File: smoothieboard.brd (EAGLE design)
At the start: 105.1 x 105.1 mm, 236 parts, among them IC1 LPC1769, IC10 LM1117-3.3V, IC11 78L12F, IC2 A4982, IC3 A4982, IC4 MCP44X1, IC5 A4982, IC6 A4982, J10 POWER_JACKSMD, J5 POWER_JACKSMD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

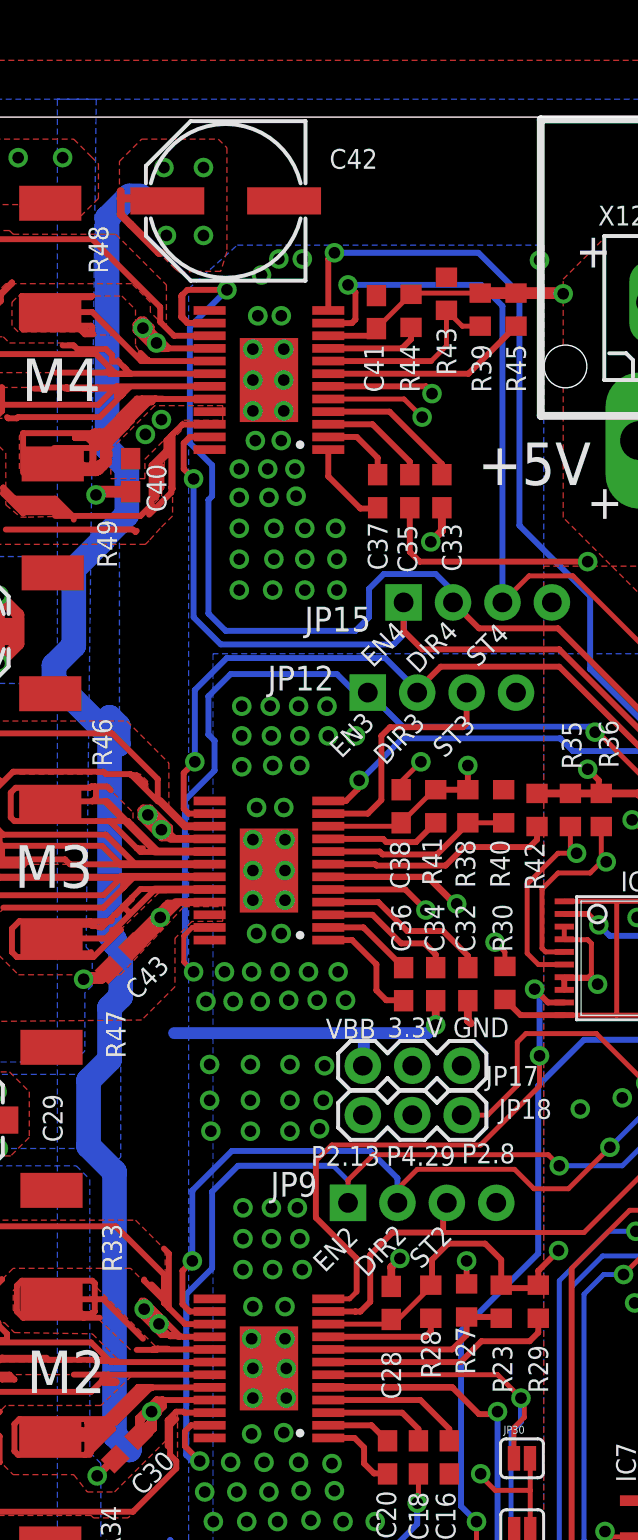
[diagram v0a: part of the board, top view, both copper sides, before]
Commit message: Moved C34 to allow heatsink to reach all four drivers from side
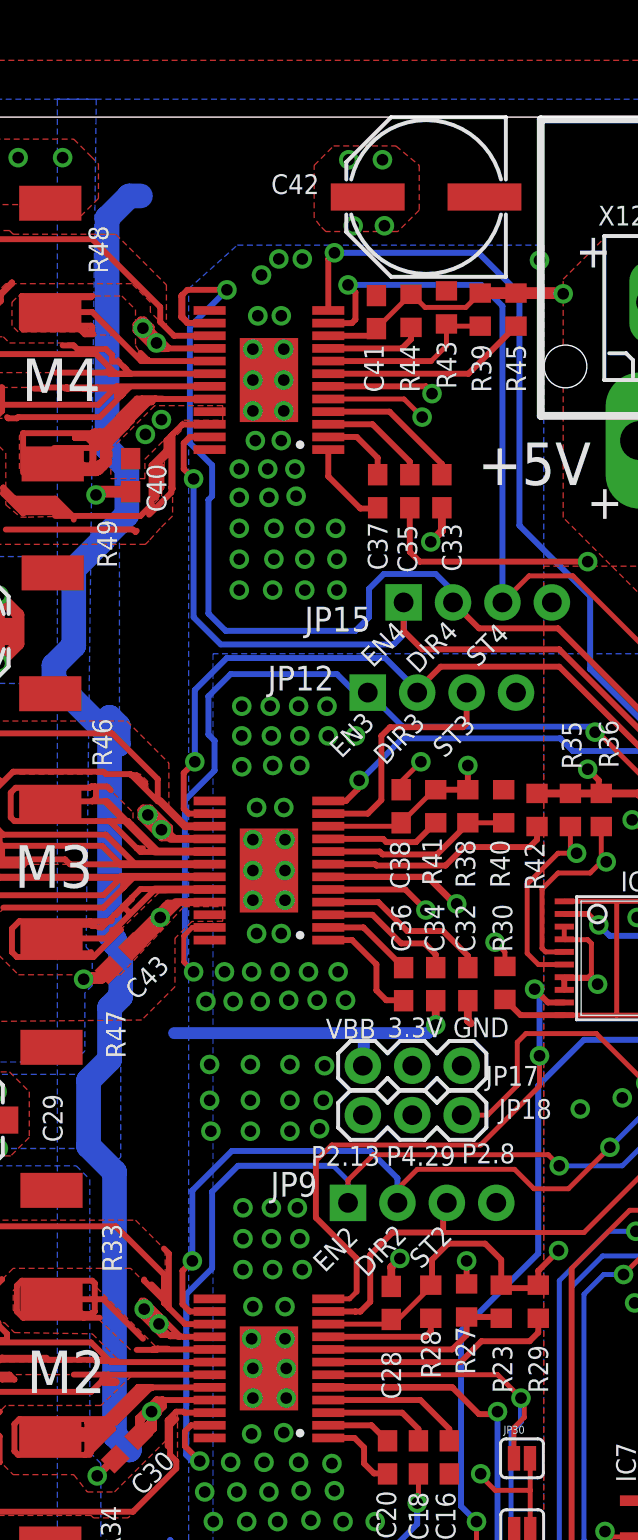
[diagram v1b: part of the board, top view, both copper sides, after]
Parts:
- moved C42 10.3 mm to (32.0, 101.0)
- moved R43 0.70 mm to (33.0, 95.3)
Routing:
- net VBB: track 332.1 -> 326.9 mm
- net N$53: track 10.3 -> 9.30 mm
- net 3.3V: track 249.6 -> 250.2 mm
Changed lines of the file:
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@@
 <setting verticaltext="up"/>
 </settings>
-<grid distance="0.25" unitdist="mm" unit="mm" style="dots" multiple="4" display="no" altdistance="0.0635" altunitdist="mm" altunit="mm"/>
+<grid distance="0.1" unitdist="mm" unit="mm" style="dots" multiple="4" display="no" altdistance="0.0635" altunitdist="mm" altunit="mm"/>
 <layers>
 <layer number="1" name="Top" color="4" fill="1" visible="yes" active="yes"/>
-<layer number="2" name="Route2" color="2" fill="1" visible="yes" active="yes"/>
+<layer number="2" name="Route2" color="2" fill="1" visible="no" active="yes"/>
 <layer number="3" name="Route3" color="4" fill="3" visible="no" active="no"/>
 <layer number="4" name="Route4" color="1" fill="4" visible="no" active="no"/>
@@
 <layer number="13" name="Route13" color="4" fill="5" visible="no" active="no"/>
 <layer number="14" name="Route14" color="1" fill="6" visible="no" active="no"/>
-<layer number="15" name="Route15" color="5" fill="1" visible="yes" active="yes"/>
+<layer number="15" name="Route15" color="5" fill="1" visible="no" active="yes"/>
 <layer number="16" name="Bottom" color="1" fill="1" visible="yes" active="yes"/>
 <layer number="17" name="Pads" color="2" fill="1" visible="yes" active="yes"/>
@@
 <attribute name="VALUE" x="29.9085" y="96.5835" size="1.27" layer="27" rot="R90"/>
 </element>
-<element name="R43" library="resistor" package="R0603" value="10K" x="33" y="96" smashed="yes" rot="R90">
-<attribute name="NAME" x="33.508" y="91.809" size="1.016" layer="25" rot="R90"/>
-<attribute name="VALUE" x="33.254" y="97.778" size="1.27" layer="27" rot="R90"/>
+<element name="R43" library="resistor" package="R0603" value="10K" x="33" y="95.3" smashed="yes" rot="R90">
+<attribute name="NAME" x="33.508" y="91.109" size="1.016" layer="25" rot="R90"/>
+<attribute name="VALUE" x="33.254" y="97.078" size="1.27" layer="27" rot="R90"/>
 </element>
 <element name="C33" library="rcl" package="C0603" value=".22uF" x="32.766" y="85.852" smashed="yes" rot="R90">
@@
 <attribute name="VALUE" x="5.126" y="76.101" size="0.4064" layer="27"/>
 </element>
-<element name="C42" library="SparkFun" package="PANASONIC_E" value="100uF" x="21.6535" y="100.7745" smashed="yes" rot="R180">
-<attribute name="NAME" x="26.9875" y="102.4255" size="1.016" layer="25"/>
-<attribute name="VALUE" x="22.9235" y="103.3145" size="0.4064" layer="27" rot="R180"/>
+<element name="C42" library="SparkFun" package="PANASONIC_E" value="100uF" x="31.9535" y="100.9745" smashed="yes" rot="R180">
+<attribute name="NAME" x="23.9875" y="101.1255" size="1.016" layer="25"/>
+<attribute name="VALUE" x="33.2235" y="103.5145" size="0.4064" layer="27" rot="R180"/>
 </element>
 <element name="U1" library="SparkFun" package="MICRO-SD-SOCKET-PP" value="USD-SOCKETNEW" x="42.037" y="16.002" rot="R180"/>
@@
 <wire x1="31.1785" y1="95.973" x2="31.164" y2="95.973" width="0.254" layer="1"/>
 <wire x1="31.164" y1="95.973" x2="29.4005" y2="94.2095" width="0.254" layer="1"/>
-<wire x1="31.242" y1="96.0365" x2="34.7345" y2="96.0365" width="0.254" layer="1"/>
 <wire x1="71.15" y1="43" x2="70.94" y2="43" width="0.254" layer="1"/>
 <wire x1="70.94" y1="43" x2="69.7865" y2="41.8465" width="0.254" layer="1"/>
@@
 <wire x1="96.25" y1="14.611" x2="94.551" y2="14.611" width="0.6096" layer="1"/>
 <wire x1="94.551" y1="14.611" x2="94.2865" y2="14.3465" width="0.6096" layer="1"/>
+<wire x1="31.242" y1="96.0365" x2="31.242" y2="95.958" width="0.254" layer="1"/>
+<wire x1="31.242" y1="95.958" x2="31.9" y2="95.3" width="0.254" layer="1"/>
+<wire x1="31.9" y1="95.3" x2="33.998" y2="95.3" width="0.254" layer="1"/>
+<wire x1="33.998" y1="95.3" x2="34.7345" y2="96.0365" width="0.254" layer="1"/>
 </signal>
 <signal name="AVCC">
@@
 <vertex x="93" y="57.5"/>
 </polygon>
-<via x="20.5105" y="102.489" extent="1-16" drill="0.6"/>
-<via x="18.4785" y="102.489" extent="1-16" drill="0.6"/>
-<via x="20.5105" y="98.9965" extent="1-16" drill="0.6"/>
-<via x="18.6055" y="98.9965" extent="1-16" drill="0.6"/>
-<polygon width="0.3048" layer="1">
-<vertex x="20.066" y="97.155"/>
-<vertex x="19.304" y="97.0915"/>
-<vertex x="19.05" y="97.282"/>
-<vertex x="16.1925" y="100.1395"/>
-<vertex x="16.1925" y="102.8065"/>
-<vertex x="17.3355" y="103.9495"/>
-<vertex x="21.2725" y="103.9495"/>
-<vertex x="21.717" y="103.505"/>
-<vertex x="21.717" y="98.171"/>
-<vertex x="21.3995" y="97.155"/>
-</polygon>
+<via x="29.7105" y="102.889" extent="1-16" drill="0.6"/>
+<via x="27.9785" y="102.889" extent="1-16" drill="0.6"/>
+<via x="29.8105" y="99.4965" extent="1-16" drill="0.6"/>
+<via x="28.2055" y="99.4965" extent="1-16" drill="0.6"/>
 <wire x1="17.018" y1="87.6935" x2="16.9545" y2="87.63" width="0.3048" layer="1"/>
 <via x="17.526" y="88.773" extent="1-16" drill="0.6"/>
@@
 <wire x1="17.78" y1="38.0365" x2="17.78" y2="38.5445" width="0.3048" layer="1"/>
 <wire x1="17.78" y1="38.5445" x2="18.161" y2="38.9255" width="0.3048" layer="1"/>
-<wire x1="17.78" y1="38.5445" x2="17.74275" y2="38.50725" width="0.3048" layer="1"/>
-<wire x1="17.74275" y1="38.50725" x2="17.3355" y2="38.1" width="0.3048" layer="1"/>
+<wire x1="17.78" y1="38.5445" x2="17.3355" y2="38.1" width="0.3048" layer="1"/>
 <wire x1="17.3355" y1="38.1" x2="17.3355" y2="37.846" width="0.3048" layer="1"/>
 <via x="18.2245" y="43.053" extent="1-16" drill="0.6"/>
@@
 <via x="8.5" y="80.5" extent="1-16" drill="0.6"/>
 <via x="8.5" y="77" extent="1-16" drill="0.6"/>
-<wire x1="16.891" y1="99.5045" x2="16.8275" y2="99.5045" width="0.3048" layer="1"/>
-<wire x1="16.8275" y1="99.5045" x2="16.764" y2="99.568" width="0.3048" layer="1"/>
-<wire x1="18.3515" y1="98.1075" x2="18.2245" y2="98.1075" width="0.4064" layer="1"/>
-<wire x1="18.2245" y1="98.1075" x2="16.764" y2="99.568" width="0.4064" layer="1"/>
-<wire x1="16.764" y1="99.568" x2="16.256" y2="100.076" width="0.4064" layer="1"/>
-<wire x1="16.256" y1="100.076" x2="16.256" y2="100.9015" width="0.4064" layer="1"/>
-<wire x1="16.256" y1="101.2825" x2="16.256" y2="100.9015" width="0.4064" layer="1"/>
-<wire x1="16.256" y1="100.9015" x2="17.2085" y2="100.9015" width="0.4064" layer="1"/>
 <wire x1="17.272" y1="101.0285" x2="16.7005" y2="101.0285" width="1.27" layer="16"/>
 <wire x1="16.7005" y1="101.0285" x2="15.5575" y2="99.8855" width="1.27" layer="16"/>
@@
 <wire x1="18.176" y1="38.9255" x2="18.2505" y2="39" width="0.254" layer="1"/>
 <wire x1="17.8435" y1="38.5445" x2="17.78" y2="38.5445" width="0.254" layer="1"/>
+<polygon width="0.4064" layer="1">
+<vertex x="26.2" y="99.9"/>
+<vertex x="26.2" y="102.6"/>
+<vertex x="27.2" y="103.6"/>
+<vertex x="30.4" y="103.6"/>
+<vertex x="31.6" y="102.6"/>
+<vertex x="31.6" y="100.3"/>
+<vertex x="30.5" y="99.2"/>
+<vertex x="26.8" y="99.2"/>
+<vertex x="26.5" y="99.5"/>
+</polygon>
 </signal>
 <signal name="P0W">
@@
 <contactref element="R39" pad="1"/>
 <wire x1="26.926" y1="92.542" x2="32.217" y2="92.542" width="0.3048" layer="1"/>
-<wire x1="34.7345" y1="94.3365" x2="33.8135" y2="94.3365" width="0.254" layer="1"/>
-<wire x1="33.8135" y1="94.3365" x2="33" y2="95.15" width="0.254" layer="1"/>
-<wire x1="33" y1="95.15" x2="33" y2="93.325" width="0.254" layer="1"/>
+<wire x1="33" y1="94.45" x2="33" y2="93.325" width="0.254" layer="1"/>
 <wire x1="33" y1="93.325" x2="32.217" y2="92.542" width="0.254" layer="1"/>
+<wire x1="34.7345" y1="94.3365" x2="33.1135" y2="94.3365" width="0.254" layer="1"/>
+<wire x1="33.1135" y1="94.3365" x2="33" y2="94.45" width="0.254" layer="1"/>
 </signal>
 <signal name="N$54">

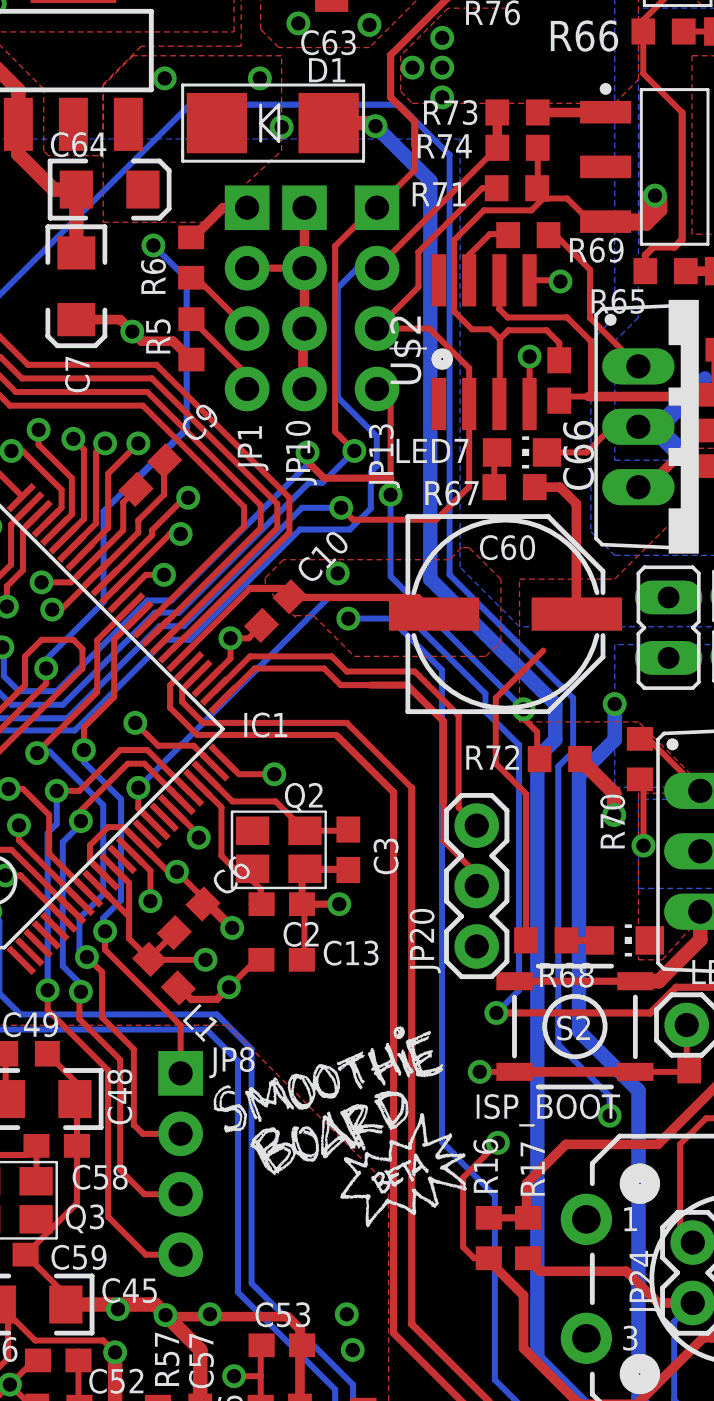
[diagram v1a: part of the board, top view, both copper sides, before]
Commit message: Fixed I2C Header Spacing
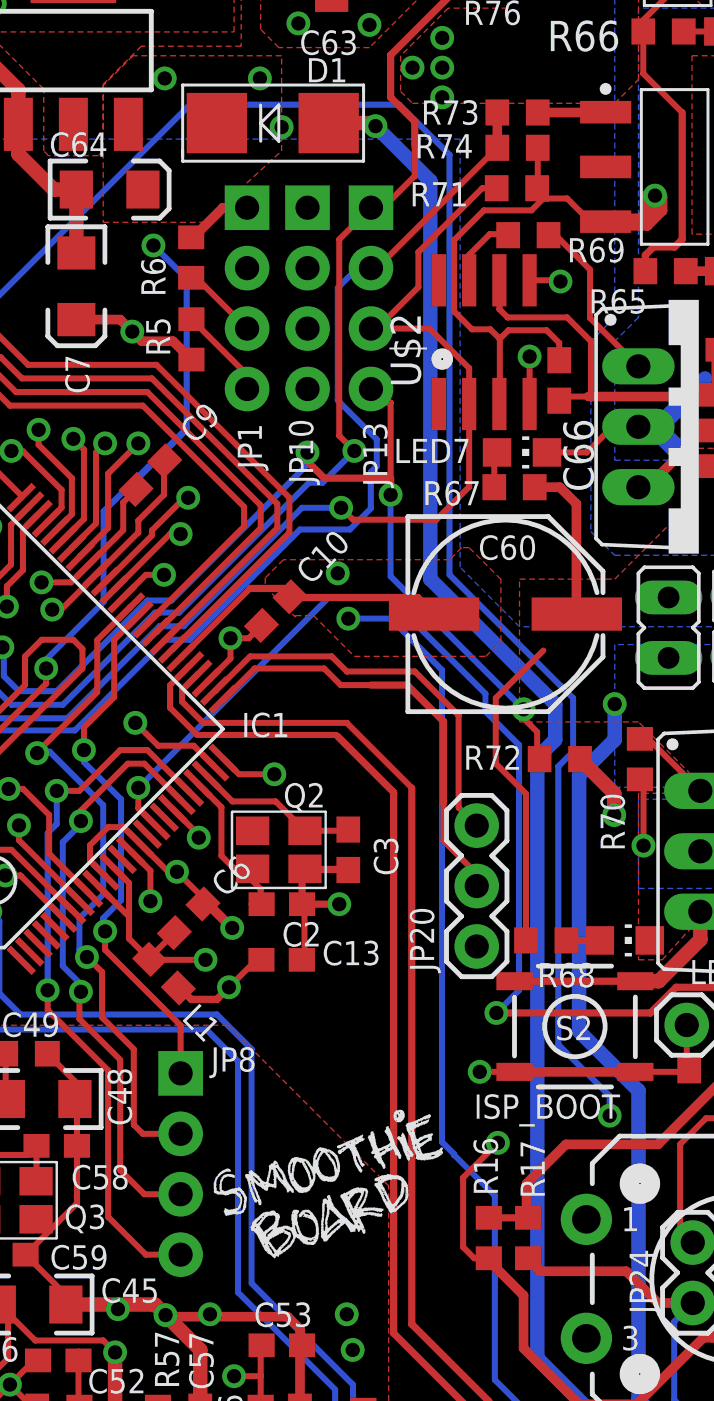
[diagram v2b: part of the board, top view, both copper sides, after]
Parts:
- moved JP13 0.25 mm to (75.8, 74.6)
- moved JP10 0.13 mm to (73.1, 74.6)
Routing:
- net GND: track 307.9 -> 297.2 mm
- net PWM1: track 51.0 -> 51.5 mm
- net P2.7: track 58.6 -> 59.1 mm
